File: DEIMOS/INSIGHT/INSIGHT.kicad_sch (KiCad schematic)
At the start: 84 parts, among them J1 Batt, J2 UFL, J3 USB_C_Receptacle_USB2.0_16P, J4 Boot, J5 GND, J6 Stack 1x04, J7 Conn_02x05_Odd_Even, J8 5V, SW3 SW_SPDT, U1 LSM6DS3, U10 453-00139R, U11 MPM3610GQV-Z, U2 MPL3115A2, U3 W25Q128JVSIQ, U5 RP2040, U6 Adafruit GPS, U7 MPM3610GQV-Z, U8 IIS2MDCTR, U9 LoRa Module, Y1 ABM8-272-T3

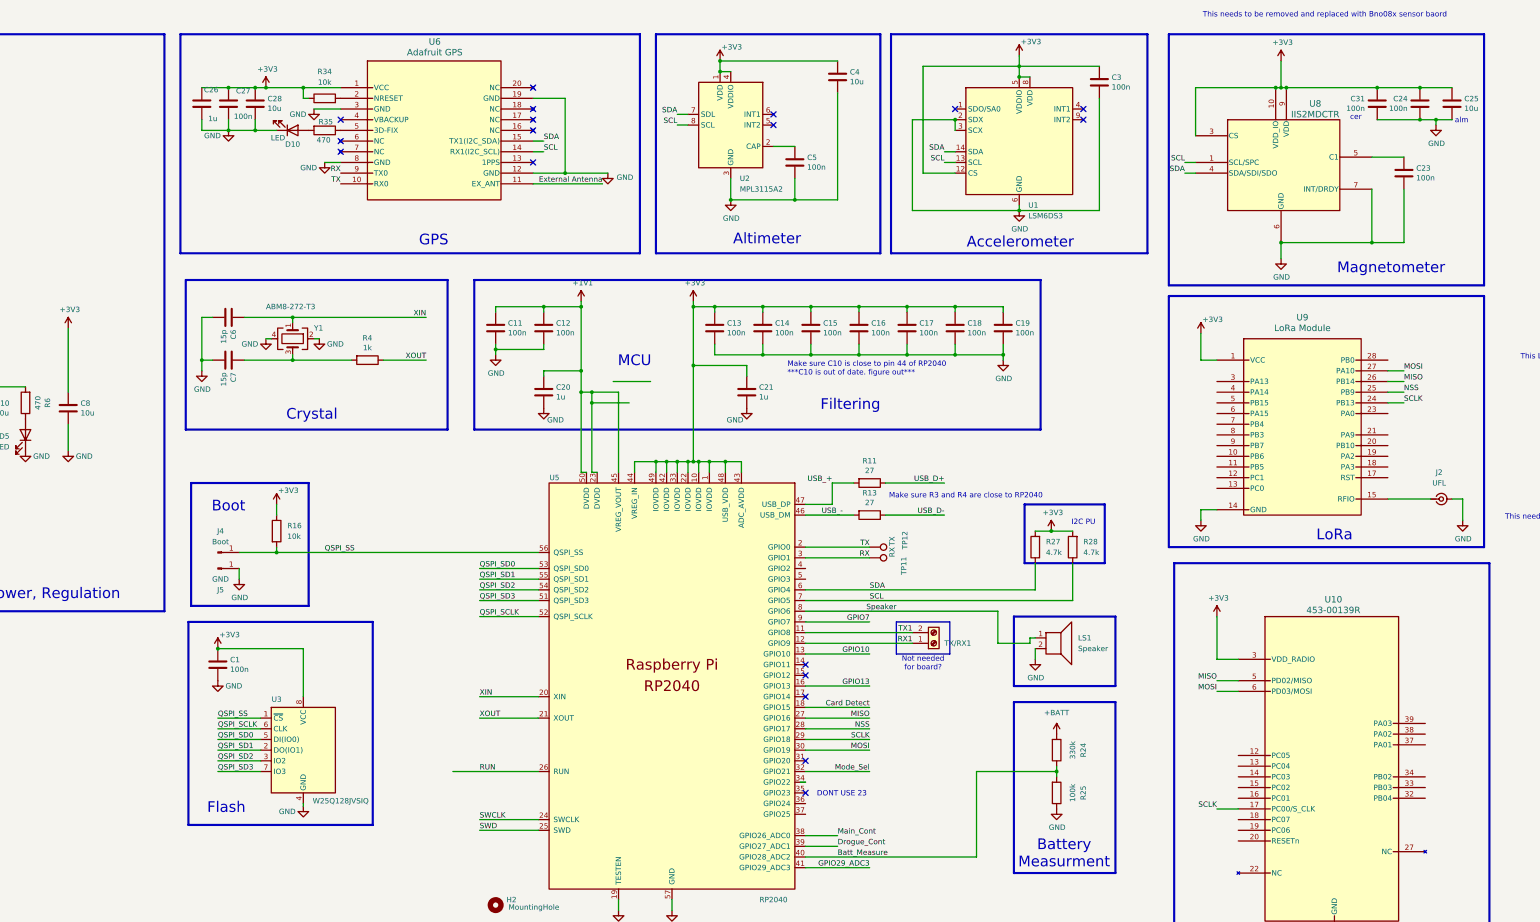
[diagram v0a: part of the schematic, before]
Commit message: Changed Magentomter to DNP and added notes about winbond flash chip have to update it to one that is currently in stock
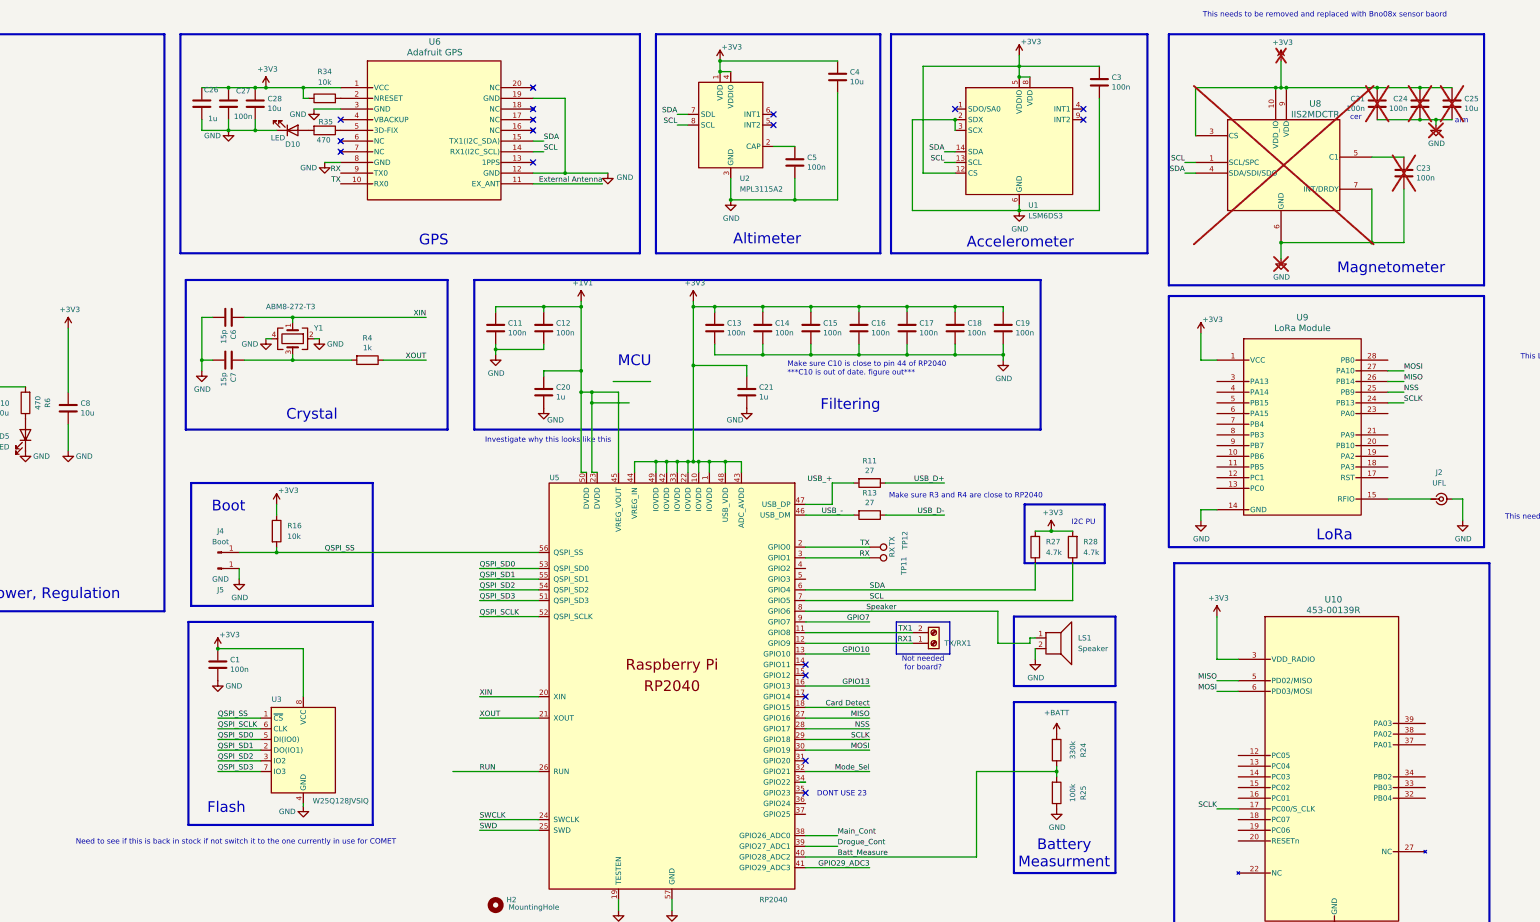
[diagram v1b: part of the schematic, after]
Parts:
- C23, C24, C25, C31, U8: now not fitted
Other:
- note added: "Investigate why this looks like this"
- note added: "Need to see if this is back in stock if not switch it to the one currently in use for COMET"
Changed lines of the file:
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@@
 	(rectangle
 		(start 473.71 393.7)
-		(end 501.65 422.91)
+		(end 516.89 422.91)
 		(stroke
 			(width 0.508)
@@
 		)
 	)
+	(text "Need to see if this is back in stock if not switch it to the one currently in use for COMET\n"
+		(exclude_from_sim no)
+		(at 446.278 479.806 0)
+		(effects
+			(font
+				(size 1.27 1.27)
+			)
+			(justify left bottom)
+		)
+	)
 	(text "Accelerometer\n"
 		(exclude_from_sim no)
@@
 		)
 	)
+	(text "Investigate why this looks like this\n"
+		(exclude_from_sim no)
+		(at 543.56 384.302 0)
+		(effects
+			(font
+				(size 1.27 1.27)
+			)
+			(justify left bottom)
+		)
+	)
 	(text "alm"
 		(exclude_from_sim no)
@@
 		(on_board yes)
 		(in_pos_files yes)
-		(dnp no)
+		(dnp yes)
 		(property "Reference" "C31"
 			(at 752.729 302.3616 0)
@@
 					(variant
 						(name "test")
+						(dnp no)
 					)
 				)
@@
 		(on_board yes)
 		(in_pos_files yes)
-		(dnp no)
+		(dnp yes)
 		(property "Reference" "C25"
 			(at 776.351 302.3616 0)
@@
 					(variant
 						(name "test")
+						(dnp no)
 					)
 				)
@@
 		(on_board yes)
 		(in_pos_files yes)
-		(dnp no)
+		(dnp yes)
 		(property "Reference" "U8"
 			(at 740.918 303.53 0)
@@
 					(variant
 						(name "test")
+						(dnp no)
 					)
 				)
@@
 		(on_board yes)
 		(in_pos_files yes)
-		(dnp no)
+		(dnp yes)
 		(property "Reference" "C24"
 			(at 762.889 302.3616 0)
@@
 					(variant
 						(name "test")
+						(dnp no)
 					)
 				)
@@
 		(on_board yes)
 		(in_pos_files yes)
-		(dnp no)
+		(dnp yes)
 		(property "Reference" "#PWR035"
 			(at 769.62 314.96 0)
@@
 		(on_board yes)
 		(in_pos_files yes)
-		(dnp no)
+		(dnp yes)
 		(property "Reference" "C23"
 			(at 764.921 318.8716 0)
@@
 					(variant
 						(name "test")
+						(dnp no)
 					)
 				)
@@
 		(on_board yes)
 		(in_pos_files yes)
-		(dnp no)
+		(dnp yes)
 		(property "Reference" "#PWR033"
 			(at 732.79 346.71 0)
@@
 		(on_board yes)
 		(in_pos_files yes)
-		(dnp no)
+		(dnp yes)
 		(property "Reference" "#PWR030"
 			(at 732.79 297.18 0)

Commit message: Made even more notes about outdated
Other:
- note added: "What is this???!!"
- note removed: "Buck Converter"
- moved on the sheet: C2, C22, C32, C33, C9, J8, R10, R12, R14, R7, R9, U11

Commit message: Added BN0085
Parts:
- removed C23, C24, C31: 100n, Capacitor_SMD:C_0402_1005Metric, symbol Device:C
- removed C25: 10u, Capacitor_SMD:C_0603_1608Metric_Pad1.08x0.95mm_HandSolder, symbol Device:C
- removed U8: IIS2MDCTR, Package_LGA:LGA-12_2x2mm_P0.5mm, symbol IIS2MDC:IIS2MDCTR
- added U4: BNO085, LGA-28_CEV, symbol 2026-09-15_01-23-40:BNO085
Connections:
- net SCL: now also U4.15 (ENV_SCL)
- net SDA: now also U4.16 (ENV_SDA)
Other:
- note added: "BN0085"
- note removed: "Magnetometer"
- note removed: "This LoRa module is not the one I want to use, I want to use the RM95W"
- note removed: "alm"
- note removed: "cer"

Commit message: Begun wiring bno085 had to import a 32.78kHz crystal ossilator for it
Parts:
- added C23, C24, C25: 100n, Capacitor_SMD:C_0402_1005Metric, symbol Device:C
- added R17: 10k, Resistor_SMD:R_0402_1005Metric, symbol Device:R
- added R29, R30: 4.7k, Resistor_SMD:R_0402_1005Metric, symbol Device:R
- added XTAL1: ABS07-32.768KHZ-7-T, XTAL_ABS07-32.768KHZ-7-T_ABR, symbol 2026-09-15_02-23-04:ABS07-32.768KHZ-7-T
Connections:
- net +3V3: now also U4.28 (VDDIO), U4.3 (VDD), C23.1, C24.1, R17.1, R29.2, R30.2
- net GND: now also U4.17 (SA0/H_MOSI), U4.2 (GND), U4.25 (GND), U4.26 (XOUT32/CLKSEL1), U4.5 (PS1), U4.6 (PS0/WAKE), C23.2, C24.2, C25.2
- net SCL: now also U4.19 (H_SCL/SCK/RX); no longer U4.15 (ENV_SCL)
- net SDA: now also U4.20 (H_SDA/H_MISO/TX); no longer U4.16 (ENV_SDA)
- net at U4.4 (BOOTN): now also R17.2
- net at U4.9 (CAP): now also C25.1
- new net: R29.1, U4.16 (ENV_SDA)
- new net: R30.1, U4.15 (ENV_SCL)
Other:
- moved on the sheet: U4

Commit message: Crystal ossilator has been connected
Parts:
- added C31, C34: 22p, Capacitor_SMD:C_0402_1005Metric, symbol Device:C
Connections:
- net GND: now also U4.10 (CLKSEL0), C31.2, C34.2; no longer U4.26 (XOUT32/CLKSEL1)
- net at U4.27 (XIN32): now also XTAL1.2, C34.1
- net at XTAL1.1: now also U4.26 (XOUT32/CLKSEL1), C31.1
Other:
- moved on the sheet: XTAL1A

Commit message: Finished Routing BNo085 had to select diffrent 32Khz ossilator due to the caps
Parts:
- removed U10: 453-00139R, 453_00140R:MOD47_RM126x_LRD, symbol 453_00140R:453-00140R
- removed XTAL1: ABS07-32.768KHZ-7-T, XTAL_ABS07-32.768KHZ-7-T_ABR, symbol 2026-09-15_02-23-04:ABS07-32.768KHZ-7-T
- added R18: 10k, Resistor_SMD:R_0402_1005Metric, symbol Device:R
- added Y2: ABS07-32.768KHZ-1-T, ABS07-32.768KHZ-1-T:XTAL_ABS07-32.768KHZ-1-T, symbol ABS07-32.768KHZ-1-T:ABS07-32.768KHZ-1-T
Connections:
- net Card Detect is gone; now on net H_INTN: U5.18 (GPIO15)
- net GPIO7 is gone; now on net NRST: U5.9 (GPIO7)
- net +3V3: now also R18.1
- net NRST: now reaches U4.11 (NRST)
- net NRST: now also R18.2
- net H_INTN: now reaches U4.14 (H_INTN)
- net at C31.1, U4.26 (XOUT32/CLKSEL1): now also Y2.1
- net at C34.1, U4.27 (XIN32): now also Y2.2
- no-connect marks 22 -> 23
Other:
- note added: "Okay need to check on H_CSN"
- note removed: "This needs to be removed and replaced with Bno08x sensor baord"
- note removed: "What is this???!!"
- moved on the sheet: C10, C2, C22, C29, C30, C32, C33, C8, C9, D1, D4, D5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

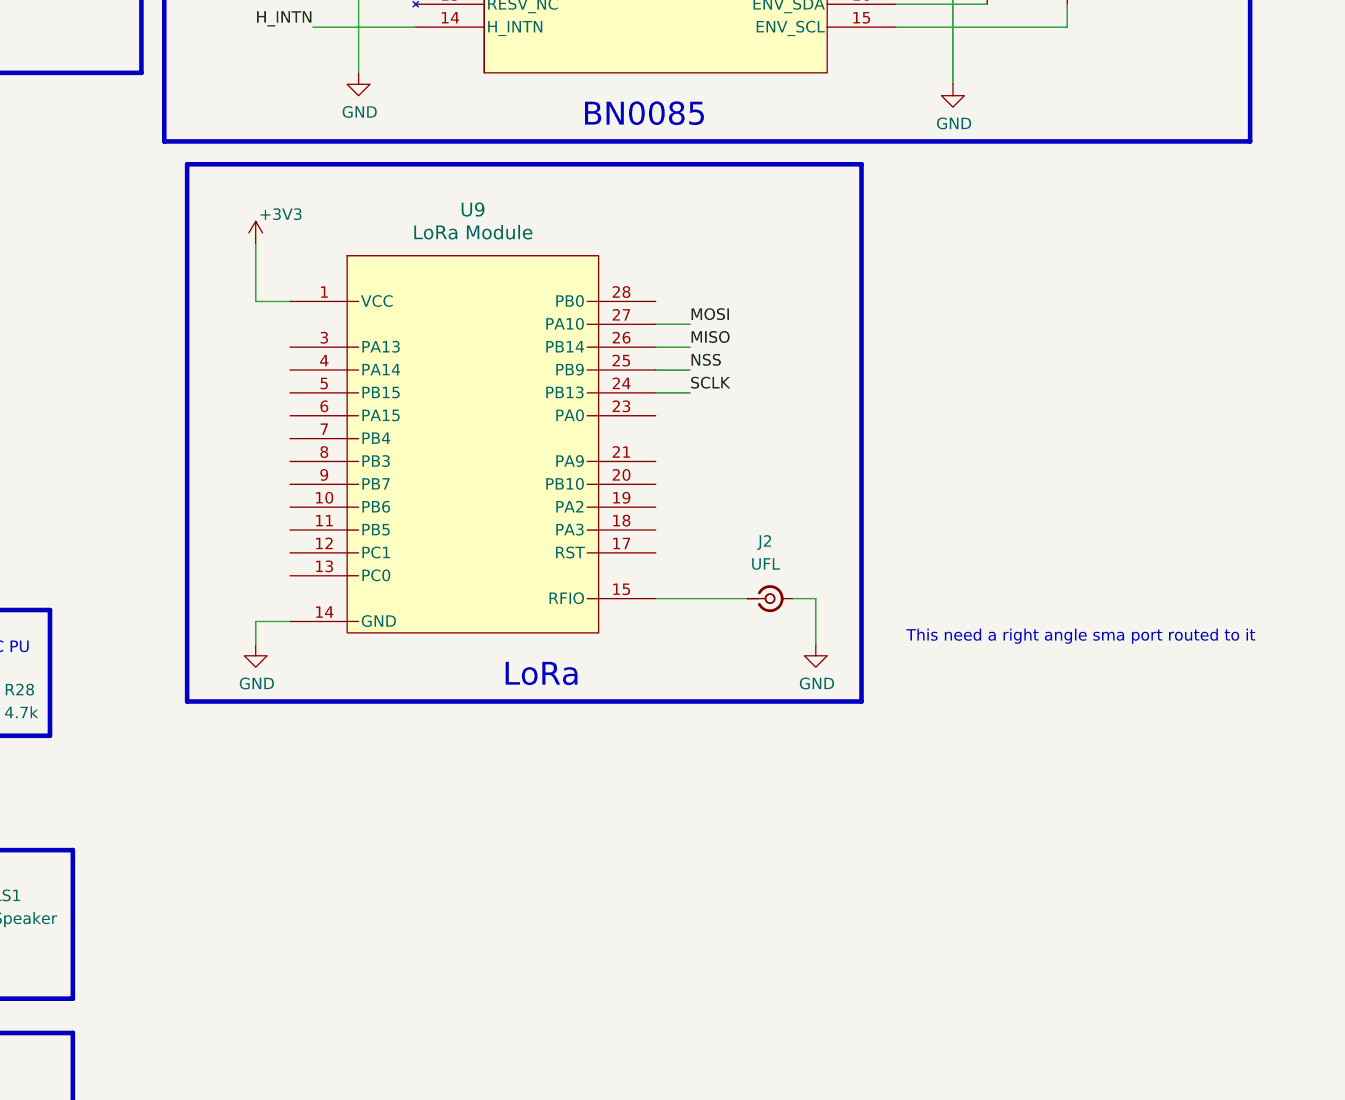
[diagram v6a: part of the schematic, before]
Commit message: Added notes about RFD900ux
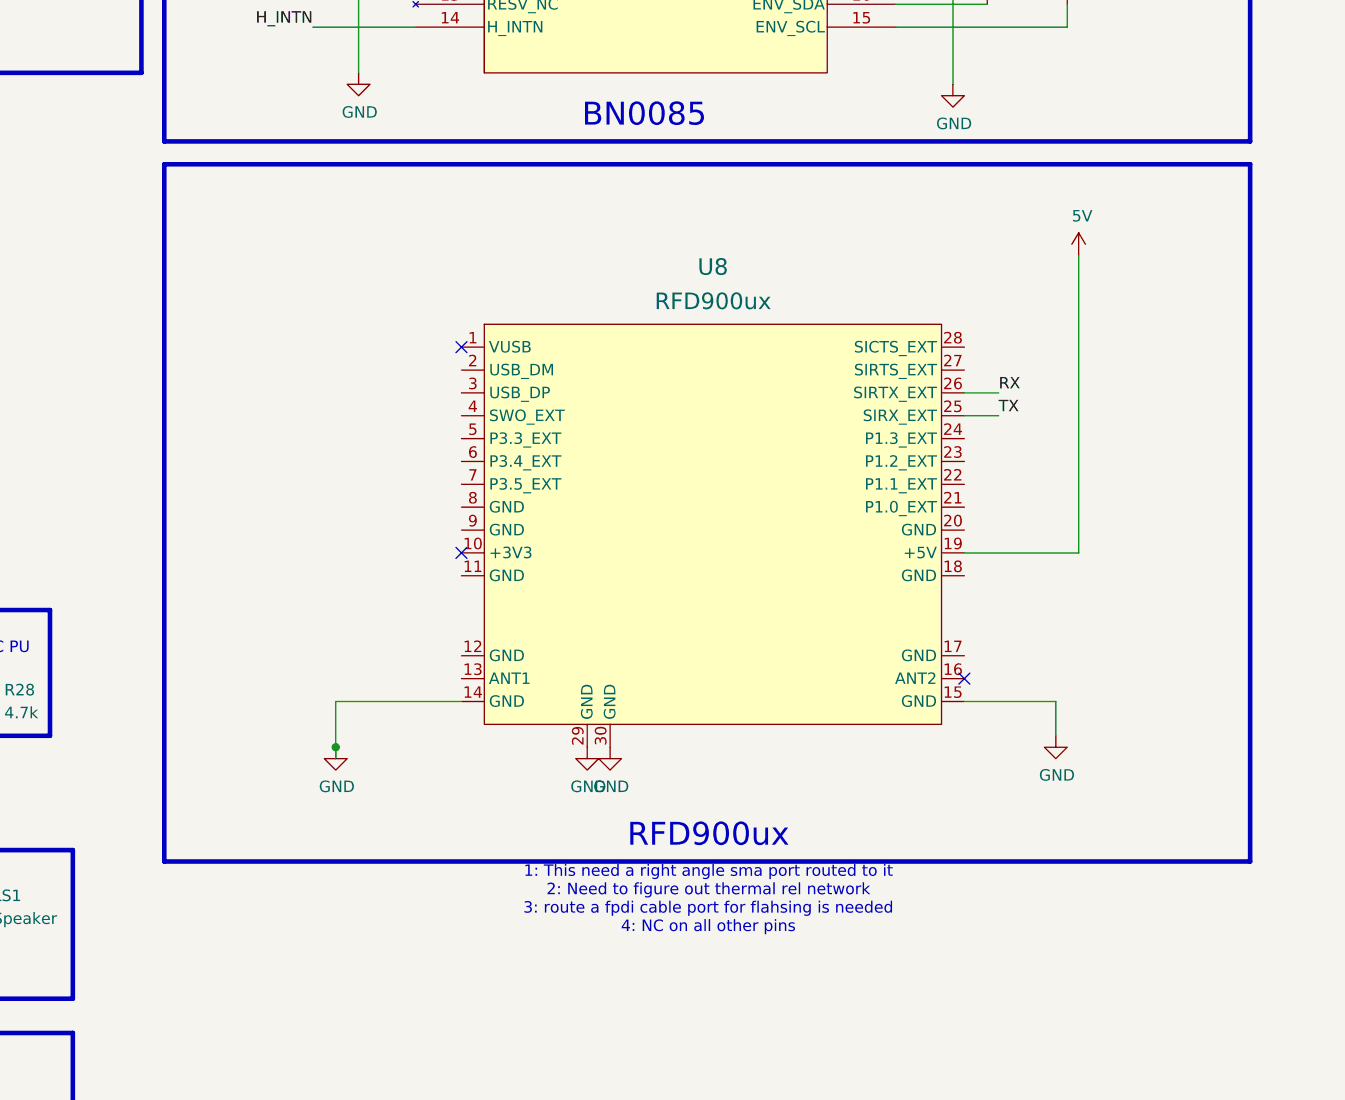
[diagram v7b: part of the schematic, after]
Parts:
- removed J2: UFL, Connector_Coaxial:U.FL_Molex_MCRF_73412-0110_Vertical, symbol Connector:Conn_Coaxial_Small
- removed U9: LoRa Module, footprints:QFN_90687_SEE, symbol 317990687:317990687
- added U8: RFD900ux, RFD900UX, symbol RFD900ux:RFD900UX
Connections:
- net 5V: now also U8.19 (+5V)
- net GND: now also U8.14 (GND), U8.15 (GND), U8.29 (GND), U8.30 (GND)
- net RX: now also U8.26 (SIRTX_EXT)
- net TX: now also U8.25 (SIRX_EXT)
- no-connect marks 23 -> 26
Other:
- note added: "1: This need a right angle sma port routed to it 2: Need to figure out thermal rel network 3: route a fpdi cable port for flahsing is needed 4: NC on all other pins"
- note added: "RFD900ux"
- note removed: "LoRa"
- note removed: "This need a right angle sma port routed to it"
